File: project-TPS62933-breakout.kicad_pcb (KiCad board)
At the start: 4 copper layers, 36 x 23 mm, 14 parts, among them J1 Conn_01x04_Pin, U1 TPS7A2033PDBVR, U2 TPS62933DRLR

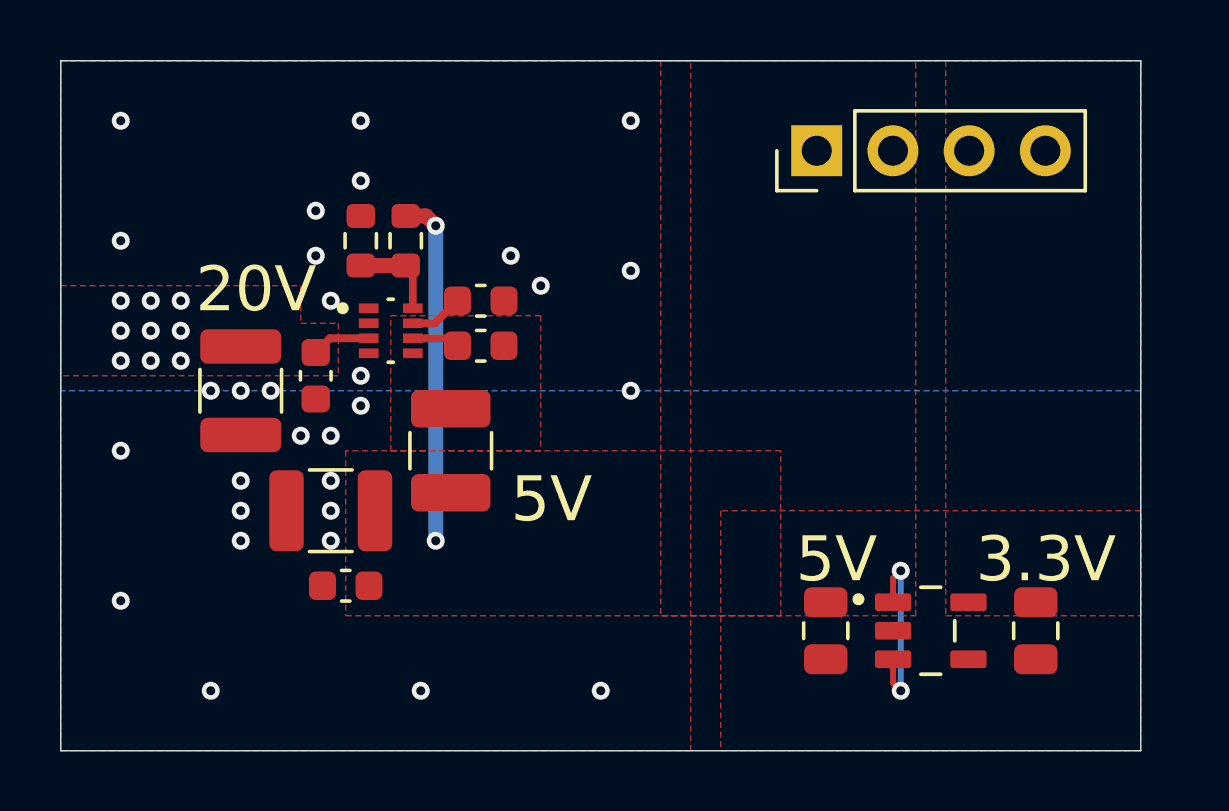
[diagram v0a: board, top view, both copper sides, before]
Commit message: Add connector silk information
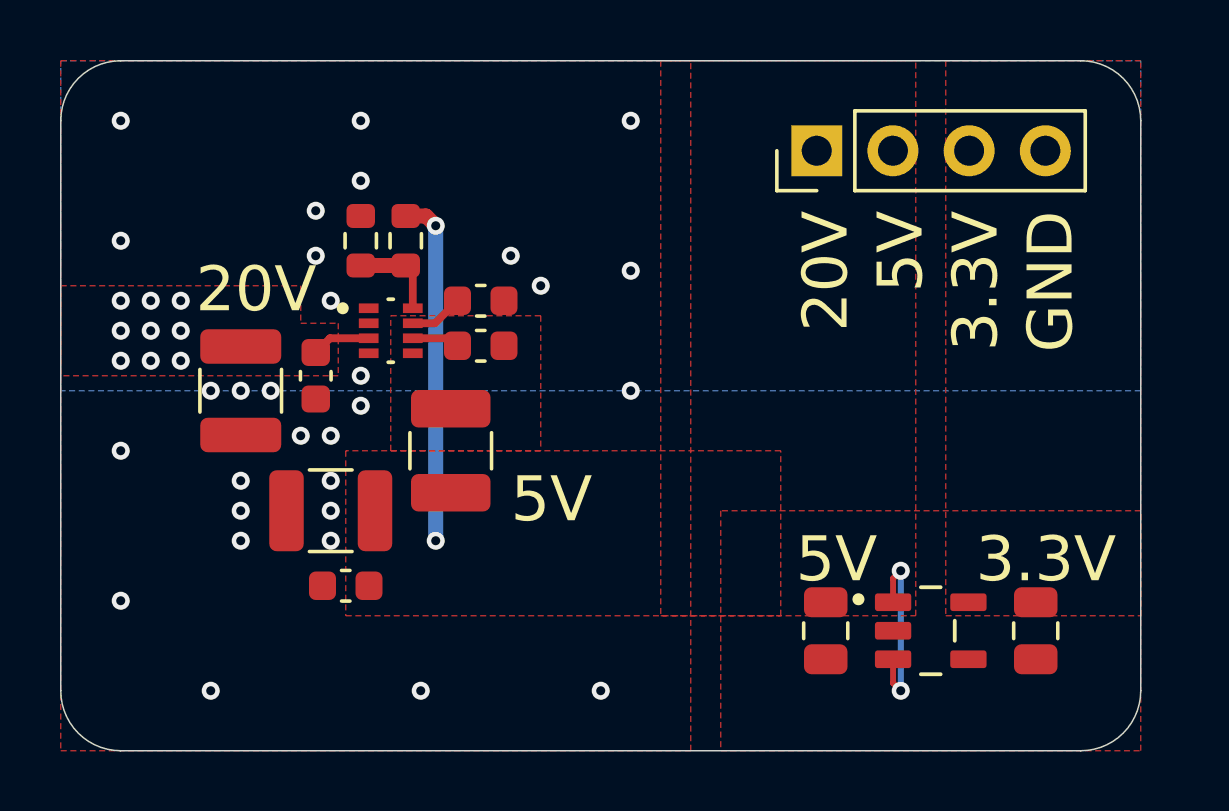
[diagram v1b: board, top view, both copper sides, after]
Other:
- outline, holes or cut-outs redrawn
- board text added: "GND"

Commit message: Add version on silkscreen
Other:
- board text added: "v1.0.0"
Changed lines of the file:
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@@
 		(layer "Edge.Cuts")
+	)
+	(gr_text "v1.0.0"
+		(at 58 40 0)
+		(layer "B.SilkS")
+		(effects
+			(font
+				(face "FreeSans")
+				(size 1.5 1.5)
+				(thickness 0.1)
+			)
+			(justify left bottom mirror)
+		)
+		(render_cache "v1.0.0" 0
+			(polygon
+				(pts
+					(xy 57.398429 39.745) (xy 57.590771 39.745) (xy 57.97875 38.642976) (xy 57.780547 38.642976) (xy 57.485258 39.536905)
+					(xy 57.172749 38.642976) (xy 56.974546 38.642976)
+				)
+			)
+			(polygon
+				(pts
+					(xy 56.412909 38.666423) (xy 56.744103 38.666423) (xy 56.744103 38.525739) (xy 56.668712 38.515289)
+					(xy 56.594039 38.501339) (xy 56.519052 38.480622) (xy 56.463468 38.453932) (xy 56.413026 38.397253)
+					(xy 56.378093 38.327158) (xy 56.352568 38.254492) (xy 56.349528 38.244371) (xy 56.227163 38.244371)
+					(xy 56.227163 39.745) (xy 56.412909 39.745)
+				)
+			)
+			(polygon
+				(pts
+					(xy 55.404675 39.533974) (xy 55.404675 39.745) (xy 55.624127 39.745) (xy 55.624127 39.533974)
+				)
+			)
+			(polygon
+				(pts
+					(xy 54.747572 38.247597) (xy 54.819958 38.261224) (xy 54.88758 38.288643) (xy 54.949651 38.328635)
+					(xy 54.97026 38.345072) (xy 55.023114 38.399087) (xy 55.065788 38.459794) (xy 55.068794 38.464892)
+					(xy 55.10236 38.53556) (xy 55.126789 38.607831) (xy 55.146022 38.683276) (xy 55.149837 38.701308)
+					(xy 55.162637 38.77687) (xy 55.171498 38.857929) (xy 55.176021 38.933362) (xy 55.177529 39.013004)
+					(xy 55.177408 39.03664) (xy 55.174488 39.127627) (xy 55.167676 39.212924) (xy 55.156971 39.292531)
+					(xy 55.142374 39.366448) (xy 55.118653 39.450842) (xy 55.08885 39.526346) (xy 55.052965 39.592958)
+					(xy 55.036943 39.617048) (xy 54.983448 39.679993) (xy 54.921813 39.72895) (xy 54.852037 39.763919)
+					(xy 54.774122 39.7849) (xy 54.688066 39.791894) (xy 54.658696 39.791126) (xy 54.57589 39.779598)
+					(xy 54.501045 39.754237) (xy 54.434159 39.715043) (xy 54.375233 39.662017) (xy 54.324267 39.595157)
+					(xy 54.316536 39.582666) (xy 54.281561 39.515073) (xy 54.252722 39.438911) (xy 54.23002 39.35418)
+					(xy 54.216275 39.280226) (xy 54.206458 39.200788) (xy 54.200567 39.115866) (xy 54.198604 39.02546)
+					(xy 54.198945 39.008607) (xy 54.388381 39.008607) (xy 54.389537 39.085246) (xy 54.394234 39.173767)
+					(xy 54.402546 39.254203) (xy 54.41447 39.326553) (xy 54.43355 39.402699) (xy 54.462386 39.476821)
+					(xy 54.492912 39.528118) (xy 54.549616 39.585163) (xy 54.619419 39.618329) (xy 54.692463 39.627763)
+					(xy 54.777532 39.612799) (xy 54.848182 39.567907) (xy 54.894321 39.510445) (xy 54.931232 39.433829)
+					(xy 54.95286 39.363797) (xy 54.969297 39.282991) (xy 54.980543 39.191411) (xy 54.986599 39.089057)
+					(xy 54.987752 39.014836) (xy 54.98746 38.977532) (xy 54.98307 38.872726) (xy 54.973412 38.778579)
+					(xy 54.958486 38.69509) (xy 54.930391 38.60035) (xy 54.89293 38.524559) (xy 54.846104 38.467715)
+					(xy 54.774402 38.423306) (xy 54.688066 38.408503) (xy 54.651776 38.410847) (xy 54.571294 38.437219)
+					(xy 54.505445 38.492892) (xy 54.463302 38.558529) (xy 54.430524 38.642919) (xy 54.412086 38.718518)
+					(xy 54.398916 38.804665) (xy 54.391014 38.901362) (xy 54.388381 39.008607) (xy 54.198945 39.008607)
+					(xy 54.200516 38.930875) (xy 54.206252 38.842392) (xy 54.215811 38.760012) (xy 54.229195 38.683734)
+					(xy 54.256441 38.580758) (xy 54.29229 38.491513) (xy 54.336743 38.415997) (xy 54.3898 38.354212)
+					(xy 54.451461 38.306157) (xy 54.521726 38.271832) (xy 54.600594 38.251236) (xy 54.688066 38.244371)
+				)
+			)
+			(polygon
+				(pts
+					(xy 53.713538 39.533974) (xy 53.713538 39.745) (xy 53.93299 39.745) (xy 53.93299 39.533974)
+				)
+			)
+			(polygon
+				(pts
+					(xy 53.056435 38.247597) (xy 53.12882 38.261224) (xy 53.196442 38.288643) (xy 53.258513 38.328635)
+					(xy 53.279123 38.345072) (xy 53.331977 38.399087) (xy 53.374651 38.459794) (xy 53.377657 38.464892)
+					(xy 53.411222 38.53556) (xy 53.435651 38.607831) (xy 53.454884 38.683276) (xy 53.4587 38.701308)
+					(xy 53.4715 38.77687) (xy 53.480361 38.857929) (xy 53.484884 38.933362) (xy 53.486392 39.013004)
+					(xy 53.48627 39.03664) (xy 53.483351 39.127627) (xy 53.476538 39.212924) (xy 53.465834 39.292531)
+					(xy 53.451236 39.366448) (xy 53.427516 39.450842) (xy 53.397713 39.526346) (xy 53.361828 39.592958)
+					(xy 53.345805 39.617048) (xy 53.29231 39.679993) (xy 53.230675 39.72895) (xy 53.1609 39.763919)
+					(xy 53.082985 39.7849) (xy 52.996929 39.791894) (xy 52.967558 39.791126) (xy 52.884753 39.779598)
+					(xy 52.809907 39.754237) (xy 52.743021 39.715043) (xy 52.684095 39.662017) (xy 52.633129 39.595157)
+					(xy 52.625398 39.582666) (xy 52.590424 39.515073) (xy 52.561585 39.438911) (xy 52.538882 39.35418)
+					(xy 52.525138 39.280226) (xy 52.51532 39.200788) (xy 52.50943 39.115866) (xy 52.507466 39.02546)
+					(xy 52.507807 39.008607) (xy 52.697243 39.008607) (xy 52.698399 39.085246) (xy 52.703097 39.173767)
+					(xy 52.711408 39.254203) (xy 52.723333 39.326553) (xy 52.742412 39.402699) (xy 52.771249 39.476821)
+					(xy 52.801774 39.528118) (xy 52.858478 39.585163) (xy 52.928282 39.618329) (xy 53.001325 39.627763)
+					(xy 53.086394 39.612799) (xy 53.157045 39.567907) (xy 53.203184 39.510445) (xy 53.240095 39.433829)
+					(xy 53.261722 39.363797) (xy 53.278159 39.282991) (xy 53.289406 39.191411) (xy 53.295462 39.089057)
+					(xy 53.296615 39.014836) (xy 53.296322 38.977532) (xy 53.291932 38.872726) (xy 53.282275 38.778579)
+					(xy 53.267349 38.69509) (xy 53.239253 38.60035) (xy 53.201792 38.524559) (xy 53.154967 38.467715)
+					(xy 53.083264 38.423306) (xy 52.996929 38.408503) (xy 52.960639 38.410847) (xy 52.880157 38.437219)
+					(xy 52.814308 38.492892) (xy 52.772165 38.558529) (xy 52.739386 38.642919) (xy 52.720949 38.718518)
+					(xy 52.707779 38.804665) (xy 52.699877 38.901362) (xy 52.697243 39.008607) (xy 52.507807 39.008607)
+					(xy 52.509378 38.930875) (xy 52.515114 38.842392) (xy 52.524674 38.760012) (xy 52.538058 38.683734)
+					(xy 52.565303 38.580758) (xy 52.601153 38.491513) (xy 52.645606 38.415997) (xy 52.698663 38.354212)
+					(xy 52.760324 38.306157) (xy 52.830588 38.271832) (xy 52.909457 38.251236) (xy 52.996929 38.244371)
+				)
+			)
+		)
 	)
 	(gr_text "20V"

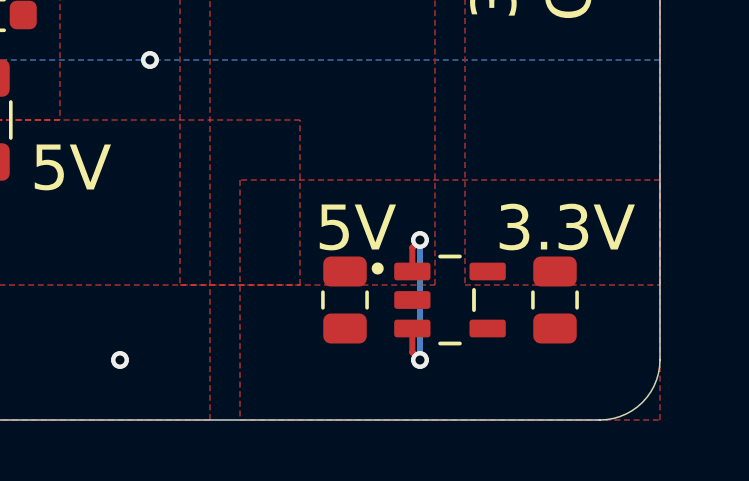
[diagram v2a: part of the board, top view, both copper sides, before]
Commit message: pcb: fix unconnected nets
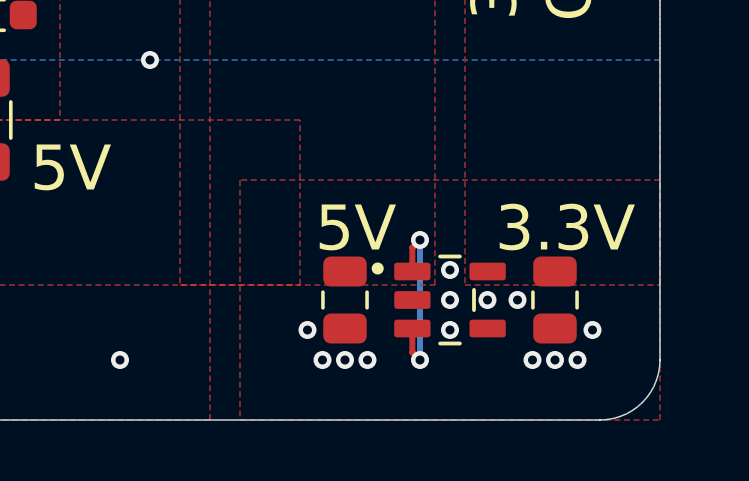
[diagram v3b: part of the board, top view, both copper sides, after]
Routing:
- net GND: vias 30 -> 43
- added copper zone on F.Cu, net Net-(U2-SW)
- removed copper zone on F.Cu, net (none)
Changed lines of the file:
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@@
+	)
+	(via
+		(at 56.25 39)
+		(size 0.6)
+		(drill 0.3)
+		(layers "F.Cu" "B.Cu")
+		(free yes)
+		(net 1)
+	)
+	(via
+		(at 56.75 38)
+		(size 0.6)
+		(drill 0.3)
+		(layers "F.Cu" "B.Cu")
+		(free yes)
+		(net 1)
+	)
+	(via
+		(at 54.75 39)
+		(size 0.6)
+		(drill 0.3)
+		(layers "F.Cu" "B.Cu")
+		(free yes)
+		(net 1)
 	)
 	(via
@@
 	)
 	(via
+		(at 54.25 37)
+		(size 0.6)
+		(drill 0.3)
+		(layers "F.Cu" "B.Cu")
+		(free yes)
+		(net 1)
+	)
+	(via
 		(at 25 31)
 		(size 0.6)
@@
 	)
 	(via
+		(at 52 36)
+		(size 0.6)
+		(drill 0.3)
+		(layers "F.Cu" "B.Cu")
+		(free yes)
+		(net 1)
+	)
+	(via
 		(at 42 29)
 		(size 0.6)
@@
 	)
 	(via
+		(at 52 37)
+		(size 0.6)
+		(drill 0.3)
+		(layers "F.Cu" "B.Cu")
+		(free yes)
+		(net 1)
+	)
+	(via
 		(at 33 22)
 		(size 0.6)
@@
 	)
 	(via
+		(at 47.75 39)
+		(size 0.6)
+		(drill 0.3)
+		(layers "F.Cu" "B.Cu")
+		(free yes)
+		(net 1)
+	)
+	(via
+		(at 47.25 38)
+		(size 0.6)
+		(drill 0.3)
+		(layers "F.Cu" "B.Cu")
+		(free yes)
+		(net 1)
+	)
+	(via
 		(at 39 25.5)
 		(size 0.6)
@@
 	)
 	(via
+		(at 53.25 37)
+		(size 0.6)
+		(drill 0.3)
+		(layers "F.Cu" "B.Cu")
+		(free yes)
+		(net 1)
+	)
+	(via
 		(at 29 32)
 		(size 0.6)
@@
 	)
 	(via
+		(at 48.5 39)
+		(size 0.6)
+		(drill 0.3)
+		(layers "F.Cu" "B.Cu")
+		(free yes)
+		(net 1)
+	)
+	(via
 		(at 42 25)
 		(size 0.6)
@@
 	)
 	(via
+		(at 52 38)
+		(size 0.6)
+		(drill 0.3)
+		(layers "F.Cu" "B.Cu")
+		(free yes)
+		(net 1)
+	)
+	(via
 		(at 33 20)
 		(size 0.6)
@@
 	)
 	(via
+		(at 49.25 39)
+		(size 0.6)
+		(drill 0.3)
+		(layers "F.Cu" "B.Cu")
+		(free yes)
+		(net 1)
+	)
+	(via
 		(at 42 20)
+		(size 0.6)
+		(drill 0.3)
+		(layers "F.Cu" "B.Cu")
+		(free yes)
+		(net 1)
+	)
+	(via
+		(at 55.5 39)
 		(size 0.6)
 		(drill 0.3)
@@
 	)
 	(zone
-		(net 0)
-		(net_name "")
+		(net 7)
+		(net_name "Net-(U2-SW)")
 		(layer "F.Cu")
 		(hatch edge 0.5)

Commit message: pcb: lower clearance on 20V poor
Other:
- board text added: "v1.0.0-2-g5650337"
- board text removed: "v1.0.0"

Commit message: pcb: update version
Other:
- board text added: "v1.0.0-3-g22dea1a"
- board text removed: "v1.0.0-2-g5650337"
